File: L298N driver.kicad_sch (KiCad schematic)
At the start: 33 parts, among them J2 Conn_01x02, J3 Conn_01x02, J4 Conn_01x05, J5 Conn_01x05, J6 Screw_Terminal_01x02, J8 Conn_01x02, J9 Conn_01x02, U1 L298N, U2 LM78M05_TO220, U3 DEV-15795, U4 74HC595, U5 L298N

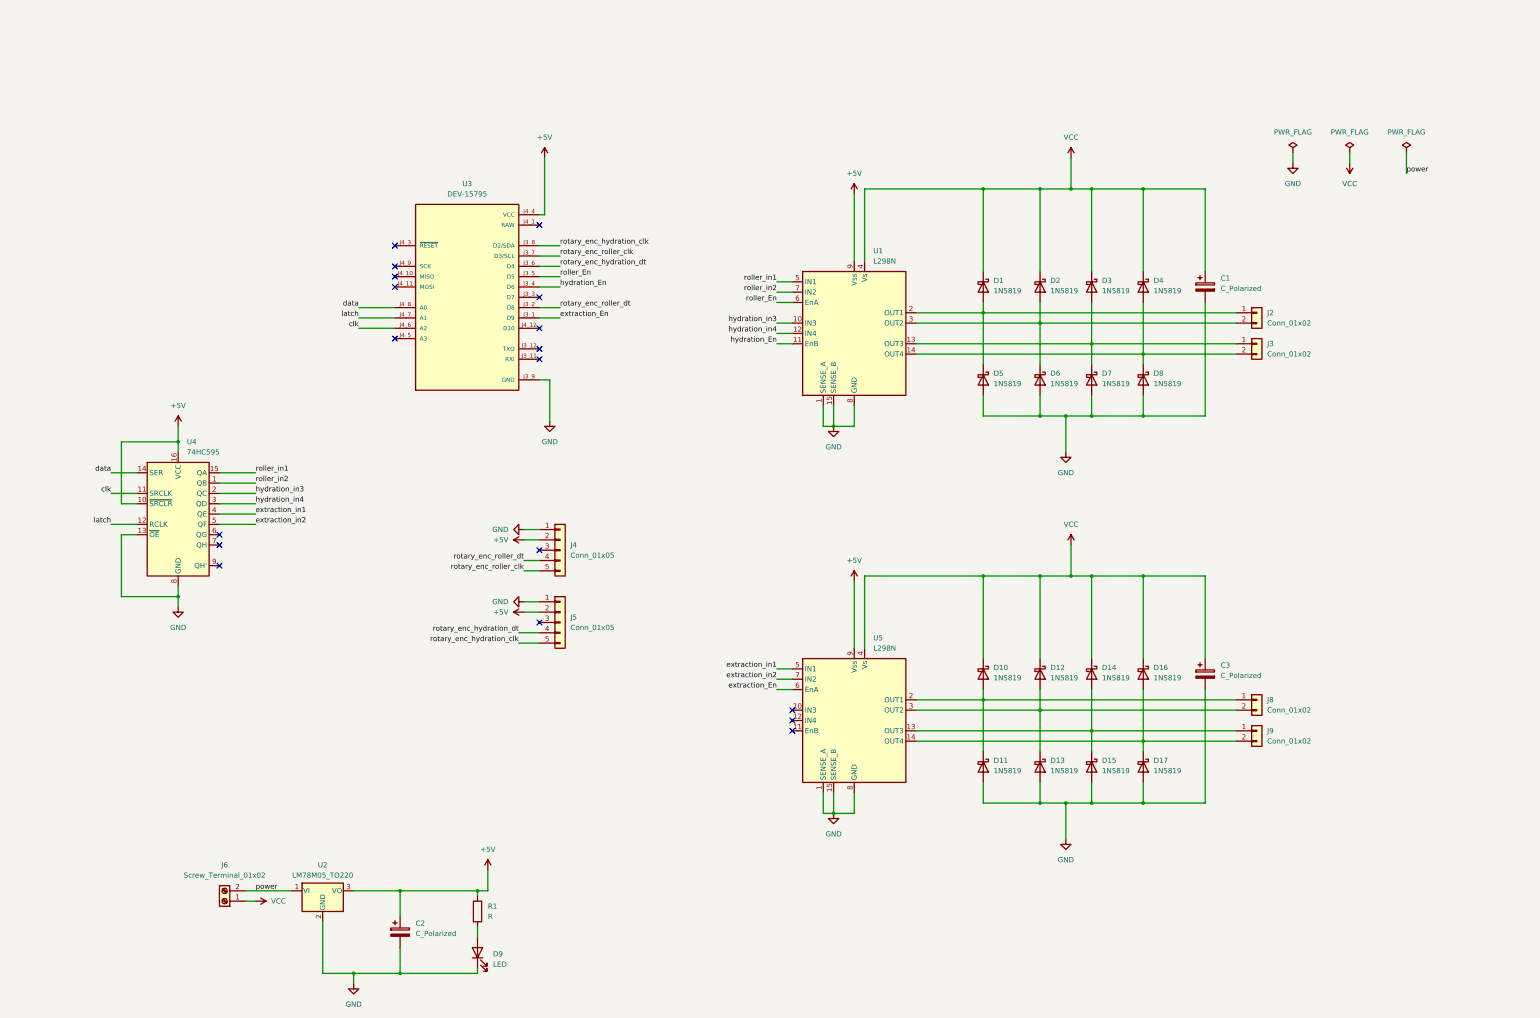
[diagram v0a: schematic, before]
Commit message: changed to fast switching diode UF4004
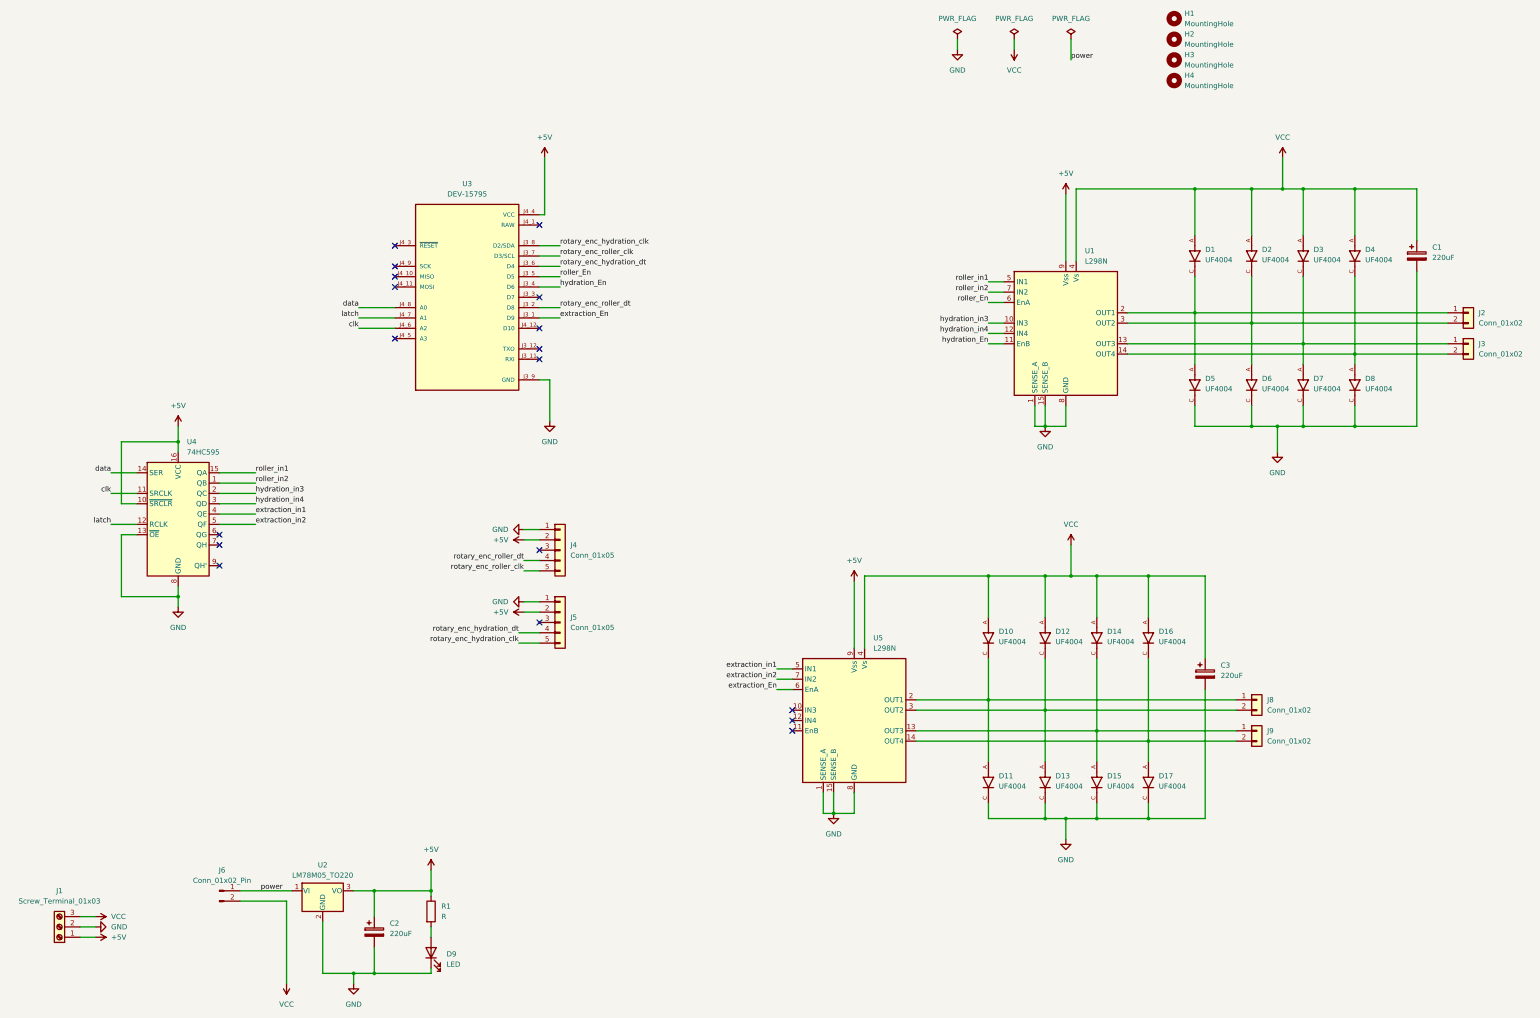
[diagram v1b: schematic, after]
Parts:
- removed J6: Screw_Terminal_01x02, TerminalBlock_Phoenix:TerminalBlock_Phoenix_MKDS-1,5-2-5.08_1x02_P5.08mm_Horizontal, symbol Connector:Screw_Terminal_01x02
- added H1, H2, H3, H4: MountingHole, MountingHole:MountingHole_3.2mm_M3_Pad_Via, symbol Mechanical:MountingHole
- added J1: Screw_Terminal_01x03, TerminalBlock_Phoenix:TerminalBlock_Phoenix_MKDS-1,5-2_1x02_P5.00mm_Horizontal, symbol Connector:Screw_Terminal_01x03
- added J6: Conn_01x02_Pin, Connector_PinHeader_2.54mm:PinHeader_1x02_P2.54mm_Vertical, symbol Connector:Conn_01x02_Pin
- C1, C3: value C_Polarized -> 220uF; footprint Capacitor_SMD:CP_Elec_5x4.4 -> Capacitor_SMD:CP_Elec_8x10
- C2: value C_Polarized -> 220uF; footprint Capacitor_SMD:CP_Elec_8x11.9 -> Capacitor_SMD:CP_Elec_8x10
- D1, D10, D11, D12, D13, D14, D15, D16, D17, D2, D3, D4, D5, D6, D7, D8: value 1N5819 -> UF4004; footprint Diode_THT:D_DO-41_SOD81_P10.16mm_Horizontal -> UF4004:DIOAD1055W87L533D272; symbol Diode:1N5819 -> UF4004:UF4004; Availability (none) -> In Stock; Check_prices (none) -> https://www.snapeda.com/parts/UF4004/Onsemi/view-part/?ref=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; Description_1 (none) -> Diode Standard 400V 1A Through Hole DO-204AL (DO-41); MANUFACTURER (none) -> NTE; MAXIMUM_PACKAGE_HEIGHT (none) -> 2.72 mm; MF (none) -> ON Semiconductor; MP (none) -> UF4004; PARTREV (none) -> N/A; Package (none) -> DO-41-2 ON Semiconductor; Price (none) -> None; STANDARD (none) -> IPC-7351B; SnapEDA_Link (none) -> https://www.snapeda.com/parts/UF4004/Onsemi/view-part/?ref=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
- J2, J3, J8, J9: footprint Connector_JST:JST_XH_S2B-XH-A-1_1x02_P2.50mm_Horizontal -> Connector_JST:JST_XH_B2B-XH-A_1x02_P2.50mm_Vertical
- J4, J5: footprint (none) -> Connector_JST:JST_XH_B5B-XH-A_1x05_P2.50mm_Vertical
- U2: footprint Package_TO_SOT_THT:TO-220-3_Horizontal_TabDown -> Package_TO_SOT_THT:TO-220-3_Vertical
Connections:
- net +5V: now also J1.1 (Pin_1)
- net GND: now also D11.C, D13.C, D15.C, D17.C, D5.C, D6.C, D7.C, D8.C, J1.2 (Pin_2); no longer D11.2 (A), D13.2 (A), D15.2 (A), D17.2 (A), D5.2 (A), D6.2 (A), D7.2 (A), D8.2 (A)
- net VCC: now also D1.A, D10.A, D12.A, D14.A, D16.A, D2.A, D3.A, D4.A, J1.3 (Pin_3), J6.2 (Pin_2); no longer D1.1 (K), D10.1 (K), D12.1 (K), D14.1 (K), D16.1 (K), D2.1 (K), D3.1 (K), D4.1 (K)
- net power: now also J6.1 (Pin_1)
- net at J8.2 (Pin_2), U5.3 (OUT2): now also D12.C, D13.A; no longer D12.2 (A), D13.1 (K)
- net at J2.1 (Pin_1), U1.2 (OUT1): now also D1.C, D5.A; no longer D1.2 (A), D5.1 (K)
- net at J2.2 (Pin_2), U1.3 (OUT2): now also D2.C, D6.A; no longer D2.2 (A), D6.1 (K)
- net at J9.1 (Pin_1), U5.13 (OUT3): now also D14.C, D15.A; no longer D14.2 (A), D15.1 (K)
- net at J8.1 (Pin_1), U5.2 (OUT1): now also D10.C, D11.A; no longer D10.2 (A), D11.1 (K)
- net at J3.2 (Pin_2), U1.14 (OUT4): now also D4.C, D8.A; no longer D4.2 (A), D8.1 (K)
- net at J3.1 (Pin_1), U1.13 (OUT3): now also D3.C, D7.A; no longer D3.2 (A), D7.1 (K)
- net at J9.2 (Pin_2), U5.14 (OUT4): now also D16.C, D17.A; no longer D16.2 (A), D17.1 (K)
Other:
- moved on the sheet: C1, C2, D9, J2, J3, R1, U1

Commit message: preliminary component placement and trace routing
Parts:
- D10: renamed from D1; value UF4004 -> UF5401; footprint UF4004:DIOAD1055W87L533D272 -> Diode_THT:D_DO-201AD_P15.24mm_Horizontal; symbol UF4004:UF4004 -> Diode:UF5401
- D11: renamed from D5; value UF4004 -> UF5401; footprint UF4004:DIOAD1055W87L533D272 -> Diode_THT:D_DO-201AD_P15.24mm_Horizontal; symbol UF4004:UF4004 -> Diode:UF5401
- D12: renamed from D2; value UF4004 -> UF5401; footprint UF4004:DIOAD1055W87L533D272 -> Diode_THT:D_DO-201AD_P15.24mm_Horizontal; symbol UF4004:UF4004 -> Diode:UF5401
- D13: renamed from D6; value UF4004 -> UF5401; footprint UF4004:DIOAD1055W87L533D272 -> Diode_THT:D_DO-201AD_P15.24mm_Horizontal; symbol UF4004:UF4004 -> Diode:UF5401
- D14: renamed from D3; value UF4004 -> UF5401; footprint UF4004:DIOAD1055W87L533D272 -> Diode_THT:D_DO-201AD_P15.24mm_Horizontal; symbol UF4004:UF4004 -> Diode:UF5401
- D15: renamed from D7; value UF4004 -> UF5401; footprint UF4004:DIOAD1055W87L533D272 -> Diode_THT:D_DO-201AD_P15.24mm_Horizontal; symbol UF4004:UF4004 -> Diode:UF5401
- D16: renamed from D4; value UF4004 -> UF5401; footprint UF4004:DIOAD1055W87L533D272 -> Diode_THT:D_DO-201AD_P15.24mm_Horizontal; symbol UF4004:UF4004 -> Diode:UF5401
- D17: renamed from D8; value UF4004 -> UF5401; footprint UF4004:DIOAD1055W87L533D272 -> Diode_THT:D_DO-201AD_P15.24mm_Horizontal; symbol UF4004:UF4004 -> Diode:UF5401
- D2: renamed from D10; value UF4004 -> UF5401; footprint UF4004:DIOAD1055W87L533D272 -> Diode_THT:D_DO-201AD_P15.24mm_Horizontal; symbol UF4004:UF4004 -> Diode:UF5401
- D3: renamed from D11; value UF4004 -> UF5401; footprint UF4004:DIOAD1055W87L533D272 -> Diode_THT:D_DO-201AD_P15.24mm_Horizontal; symbol UF4004:UF4004 -> Diode:UF5401
- D4: renamed from D12; value UF4004 -> UF5401; footprint UF4004:DIOAD1055W87L533D272 -> Diode_THT:D_DO-201AD_P15.24mm_Horizontal; symbol UF4004:UF4004 -> Diode:UF5401
- D5: renamed from D13; value UF4004 -> UF5401; footprint UF4004:DIOAD1055W87L533D272 -> Diode_THT:D_DO-201AD_P15.24mm_Horizontal; symbol UF4004:UF4004 -> Diode:UF5401
- D6: renamed from D14; value UF4004 -> UF5401; footprint UF4004:DIOAD1055W87L533D272 -> Diode_THT:D_DO-201AD_P15.24mm_Horizontal; symbol UF4004:UF4004 -> Diode:UF5401
- D7: renamed from D15; value UF4004 -> UF5401; footprint UF4004:DIOAD1055W87L533D272 -> Diode_THT:D_DO-201AD_P15.24mm_Horizontal; symbol UF4004:UF4004 -> Diode:UF5401
- D8: renamed from D16; value UF4004 -> UF5401; footprint UF4004:DIOAD1055W87L533D272 -> Diode_THT:D_DO-201AD_P15.24mm_Horizontal; symbol UF4004:UF4004 -> Diode:UF5401
- D9: renamed from D17; value UF4004 -> UF5401; footprint UF4004:DIOAD1055W87L533D272 -> Diode_THT:D_DO-201AD_P15.24mm_Horizontal; symbol UF4004:UF4004 -> Diode:UF5401
- J1: footprint TerminalBlock_Phoenix:TerminalBlock_Phoenix_MKDS-1,5-2_1x02_P5.00mm_Horizontal -> TerminalBlock_Phoenix:TerminalBlock_Phoenix_MKDS-1,5-3-5.08_1x03_P5.08mm_Horizontal
- U2: footprint Package_TO_SOT_THT:TO-220-3_Vertical -> Package_TO_SOT_THT:TO-220-3_Horizontal_TabDown
- renumbered C2 to C1, C3 to C2, C1 to C3, D9 to D1, J6 to J2, J4 to J3, J5 to J4, J8 to J5, J9 to J6, J2 to J7, J3 to J8, U4 to U1, U5 to U4, U1 to U5
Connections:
- net GND: now also D11.2 (A), D13.2 (A), D15.2 (A), D17.2 (A), D3.2 (A), D5.2 (A), D7.2 (A), D9.2 (A); no longer D11.C, D13.C, D15.C, D17.C, D3.C, D5.C, D7.C, D9.C
- net VCC: now also D10.1 (K), D12.1 (K), D14.1 (K), D16.1 (K), D2.1 (K), D4.1 (K), D6.1 (K), D8.1 (K); no longer D10.A, D12.A, D14.A, D16.A, D2.A, D4.A, D6.A, D8.A
- net at J5.2 (Pin_2), U4.3 (OUT2): now also D4.2 (A), D5.1 (K); no longer D4.C, D5.A
- net at J7.1 (Pin_1), U5.2 (OUT1): now also D10.2 (A), D11.1 (K); no longer D10.C, D11.A
- net at J7.2 (Pin_2), U5.3 (OUT2): now also D12.2 (A), D13.1 (K); no longer D12.C, D13.A
- net at J6.1 (Pin_1), U4.13 (OUT3): now also D6.2 (A), D7.1 (K); no longer D6.C, D7.A
- net at J5.1 (Pin_1), U4.2 (OUT1): now also D2.2 (A), D3.1 (K); no longer D2.C, D3.A
- net at J8.2 (Pin_2), U5.14 (OUT4): now also D16.2 (A), D17.1 (K); no longer D16.C, D17.A
- net at J8.1 (Pin_1), U5.13 (OUT3): now also D14.2 (A), D15.1 (K); no longer D14.C, D15.A
- net at J6.2 (Pin_2), U4.14 (OUT4): now also D8.2 (A), D9.1 (K); no longer D8.C, D9.A

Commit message: initial component layout and smd diode
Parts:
- D10, D11, D12, D13, D14, D15, D16, D17, D2, D3, D4, D5, D6, D7, D8, D9: value UF5401 -> SS34; footprint Diode_THT:D_DO-201AD_P15.24mm_Horizontal -> Diode_SMD:D_SMA; symbol Diode:UF5401 -> Diode:SS34
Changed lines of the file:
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@@
 	)
 	(symbol
-		(lib_id "Diode:UF5401")
+		(lib_id "Diode:SS34")
 		(at 279.4 207.01 270)
 		(unit 1)
@@
 			)
 		)
-		(property "Value" "UF5401"
+		(property "Value" "SS34"
 			(at 281.94 207.9624 90)
 			(effects
@@
 			)
 		)
-		(property "Footprint" "Diode_THT:D_DO-201AD_P15.24mm_Horizontal"
+		(property "Footprint" "Diode_SMD:D_SMA"
 			(at 274.955 207.01 0)
 			(effects
@@
 	)
 	(symbol
-		(lib_id "Diode:UF5401")
+		(lib_id "Diode:SS34")
 		(at 316.23 109.22 270)
 		(unit 1)
@@
 			)
 		)
-		(property "Value" "UF5401"
+		(property "Value" "SS34"
 			(at 318.77 110.1724 90)
 			(effects
@@
 			)
 		)
-		(property "Footprint" "Diode_THT:D_DO-201AD_P15.24mm_Horizontal"
+		(property "Footprint" "Diode_SMD:D_SMA"
 			(at 311.785 109.22 0)
 			(effects
@@
 	)
 	(symbol
-		(lib_id "Diode:UF5401")
+		(lib_id "Diode:SS34")
 		(at 292.1 171.45 270)
 		(unit 1)
@@
 			)
 		)
-		(property "Value" "UF5401"
+		(property "Value" "SS34"
 			(at 294.64 172.4024 90)
 			(effects
@@
 			)
 		)
-		(property "Footprint" "Diode_THT:D_DO-201AD_P15.24mm_Horizontal"
+		(property "Footprint" "Diode_SMD:D_SMA"
 			(at 287.655 171.45 0)
 			(effects
@@
 	)
 	(symbol
-		(lib_id "Diode:UF5401")
+		(lib_id "Diode:SS34")
 		(at 279.4 171.45 270)
 		(unit 1)
@@
 			)
 		)
-		(property "Value" "UF5401"
+		(property "Value" "SS34"
 			(at 281.94 172.4024 90)
 			(effects
@@
 			)
 		)
-		(property "Footprint" "Diode_THT:D_DO-201AD_P15.24mm_Horizontal"
+		(property "Footprint" "Diode_SMD:D_SMA"
 			(at 274.955 171.45 0)
 			(effects
@@
 	)
 	(symbol
-		(lib_id "Diode:UF5401")
+		(lib_id "Diode:SS34")
 		(at 330.2 77.47 270)
 		(unit 1)
@@
 			)
 		)
-		(property "Value" "UF5401"
+		(property "Value" "SS34"
 			(at 332.74 78.4224 90)
 			(effects
@@
 			)
 		)
-		(property "Footprint" "Diode_THT:D_DO-201AD_P15.24mm_Horizontal"
+		(property "Footprint" "Diode_SMD:D_SMA"
 			(at 325.755 77.47 0)
 			(effects
@@
 	)
 	(symbol
-		(lib_id "Diode:UF5401")
+		(lib_id "Diode:SS34")
 		(at 265.43 171.45 270)
 		(unit 1)
@@
 			)
 		)
-		(property "Value" "UF5401"
+		(property "Value" "SS34"
 			(at 267.97 172.4024 90)
 			(effects
@@
 			)
 		)
-		(property "Footprint" "Diode_THT:D_DO-201AD_P15.24mm_Horizontal"
+		(property "Footprint" "Diode_SMD:D_SMA"
 			(at 260.985 171.45 0)
 			(effects
@@
 	)
 	(symbol
-		(lib_id "Diode:UF5401")
+		(lib_id "Diode:SS34")
 		(at 355.6 77.47 270)
 		(unit 1)
@@
 			)
 		)
-		(property "Value" "UF5401"
+		(property "Value" "SS34"
 			(at 358.14 78.4224 90)
 			(effects
@@
 			)
 		)
-		(property "Footprint" "Diode_THT:D_DO-201AD_P15.24mm_Horizontal"
+		(property "Footprint" "Diode_SMD:D_SMA"
 			(at 351.155 77.47 0)
 			(effects
@@
 	)
 	(symbol
-		(lib_id "Diode:UF5401")
+		(lib_id "Diode:SS34")
 		(at 355.6 109.22 270)
 		(unit 1)
@@
 			)
 		)
-		(property "Value" "UF5401"
+		(property "Value" "SS34"
 			(at 358.14 110.1724 90)
 			(effects
@@
 			)
 		)
-		(property "Footprint" "Diode_THT:D_DO-201AD_P15.24mm_Horizontal"
+		(property "Footprint" "Diode_SMD:D_SMA"
 			(at 351.155 109.22 0)
 			(effects
@@
 	)
 	(symbol
-		(lib_id "Diode:UF5401")
+		(lib_id "Diode:SS34")
 		(at 304.8 207.01 270)
 		(unit 1)
@@
 			)
 		)
-		(property "Value" "UF5401"
+		(property "Value" "SS34"
 			(at 307.34 207.9624 90)
 			(effects
@@
 			)
 		)
-		(property "Footprint" "Diode_THT:D_DO-201AD_P15.24mm_Horizontal"
+		(property "Footprint" "Diode_SMD:D_SMA"
 			(at 300.355 207.01 0)
 			(effects
@@
 	)
 	(symbol
-		(lib_id "Diode:UF5401")
+		(lib_id "Diode:SS34")
 		(at 316.23 77.47 270)
 		(unit 1)
@@
 			)
 		)
-		(property "Value" "UF5401"
+		(property "Value" "SS34"
 			(at 318.77 78.4224 90)
 			(effects
@@
 			)
 		)
-		(property "Footprint" "Diode_THT:D_DO-201AD_P15.24mm_Horizontal"
+		(property "Footprint" "Diode_SMD:D_SMA"
 			(at 311.785 77.47 0)
 			(effects
@@
 	)
 	(symbol
-		(lib_id "Diode:UF5401")
+		(lib_id "Diode:SS34")
 		(at 330.2 109.22 270)
 		(unit 1)
@@
 			)
 		)
-		(property "Value" "UF5401"
+		(property "Value" "SS34"
 			(at 332.74 110.1724 90)
 			(effects
@@
 			)
 		)
-		(property "Footprint" "Diode_THT:D_DO-201AD_P15.24mm_Horizontal"
+		(property "Footprint" "Diode_SMD:D_SMA"
 			(at 325.755 109.22 0)
 			(effects
@@
 	)
 	(symbol
-		(lib_id "Diode:UF5401")
+		(lib_id "Diode:SS34")
 		(at 342.9 77.47 270)
 		(unit 1)
@@
 			)
 		)
-		(property "Value" "UF5401"
+		(property "Value" "SS34"
 			(at 345.44 78.4224 90)
 			(effects
@@
 			)
 		)
-		(property "Footprint" "Diode_THT:D_DO-201AD_P15.24mm_Horizontal"
+		(property "Footprint" "Diode_SMD:D_SMA"
 			(at 338.455 77.47 0)
 			(effects
@@
 	)
 	(symbol
-		(lib_id "Diode:UF5401")
+		(lib_id "Diode:SS34")
 		(at 304.8 171.45 270)
 		(unit 1)
@@
 			)
 		)
-		(property "Value" "UF5401"
+		(property "Value" "SS34"
 			(at 307.34 172.4024 90)
 			(effects
@@
 			)
 		)
-		(property "Footprint" "Diode_THT:D_DO-201AD_P15.24mm_Horizontal"
+		(property "Footprint" "Diode_SMD:D_SMA"
 			(at 300.355 171.45 0)
 			(effects
@@
 	)
 	(symbol
-		(lib_id "Diode:UF5401")
+		(lib_id "Diode:SS34")
 		(at 292.1 207.01 270)
 		(unit 1)
@@
 			)
 		)
-		(property "Value" "UF5401"
+		(property "Value" "SS34"
 			(at 294.64 207.9624 90)
 			(effects
@@
 			)
 		)
-		(property "Footprint" "Diode_THT:D_DO-201AD_P15.24mm_Horizontal"
+		(property "Footprint" "Diode_SMD:D_SMA"
 			(at 287.655 207.01 0)
 			(effects
@@
 	)
 	(symbol
-		(lib_id "Diode:UF5401")
+		(lib_id "Diode:SS34")
 		(at 342.9 109.22 270)
 		(unit 1)
@@
 			)
 		)
-		(property "Value" "UF5401"
+		(property "Value" "SS34"
 			(at 345.44 110.1724 90)
 			(effects
@@
 			)
 		)
-		(property "Footprint" "Diode_THT:D_DO-201AD_P15.24mm_Horizontal"
+		(property "Footprint" "Diode_SMD:D_SMA"
 			(at 338.455 109.22 0)
 			(effects
@@
 	)
 	(symbol
-		(lib_id "Diode:UF5401")
+		(lib_id "Diode:SS34")
 		(at 265.43 207.01 270)
 		(unit 1)
@@
 			)
 		)
-		(property "Value" "UF5401"
+		(property "Value" "SS34"
 			(at 267.97 207.9624 90)
 			(effects
@@
 			)
 		)
-		(property "Footprint" "Diode_THT:D_DO-201AD_P15.24mm_Horizontal"
+		(property "Footprint" "Diode_SMD:D_SMA"
 			(at 260.985 207.01 0)
 			(effects

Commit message: correct shift register to DIP-16 and power net trace width
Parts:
- U1: footprint Package_DIP:DIP-18_W7.62mm_Socket -> Package_DIP:DIP-16_W7.62mm_Socket
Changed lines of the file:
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@@
 	)
 	(no_connect
+		(at 76.2 153.67)
+	)
+	(no_connect
 		(at 154.94 87.63)
 	)
@@
 	)
 	(no_connect
-		(at 76.2 153.67)
-	)
-	(no_connect
 		(at 154.94 69.85)
 	)
@@
 			)
 		)
-		(property "Footprint" "Package_DIP:DIP-18_W7.62mm_Socket"
+		(property "Footprint" "Package_DIP:DIP-16_W7.62mm_Socket"
 			(at 66.04 140.97 0)
 			(effects
